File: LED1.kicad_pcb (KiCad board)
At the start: 2 copper layers, 45.7 x 30.5 mm, 11 parts, among them J1 Conn_01x02_Pin, SW1 Tactile_Switch_2-pin - Red, SW2 Tactile_Switch_2-pin - Yellow, SW3 Tactile_Switch_2-pin - Green

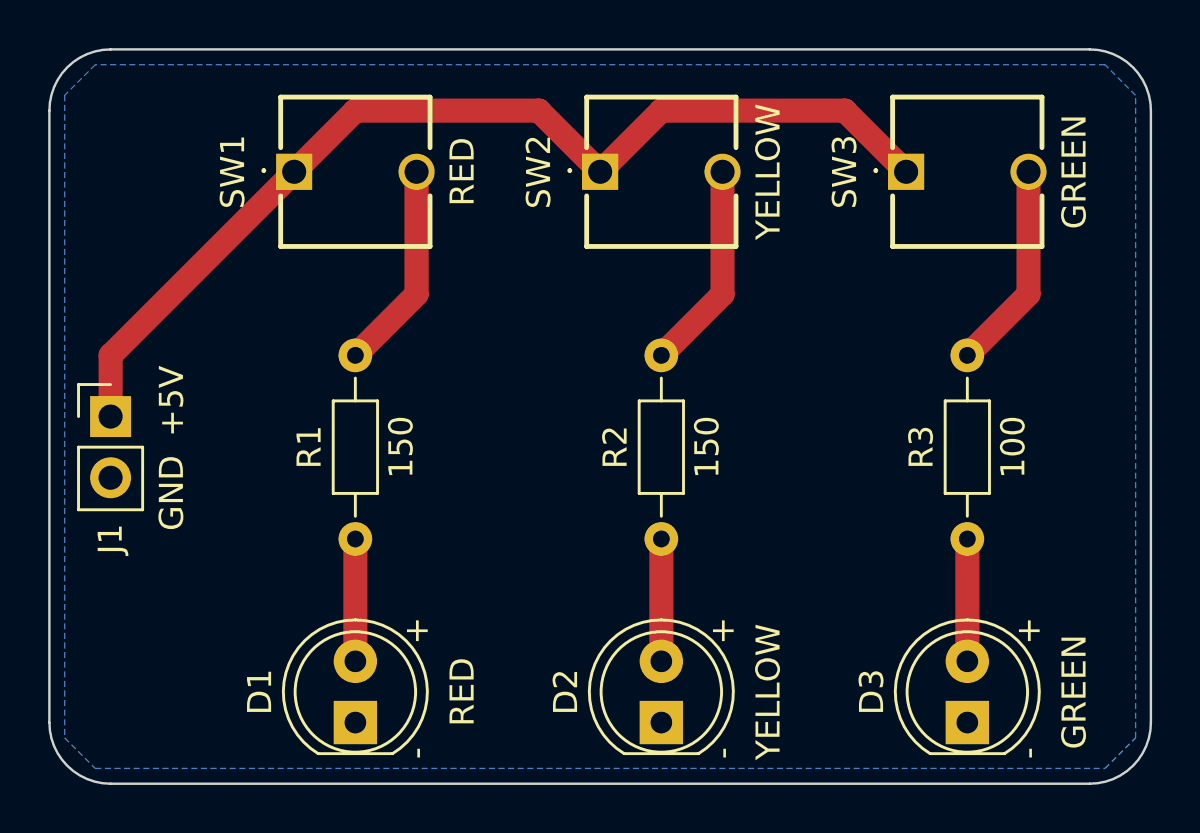
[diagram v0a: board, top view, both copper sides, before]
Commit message: Improved the layout by rotating the tactile switches.
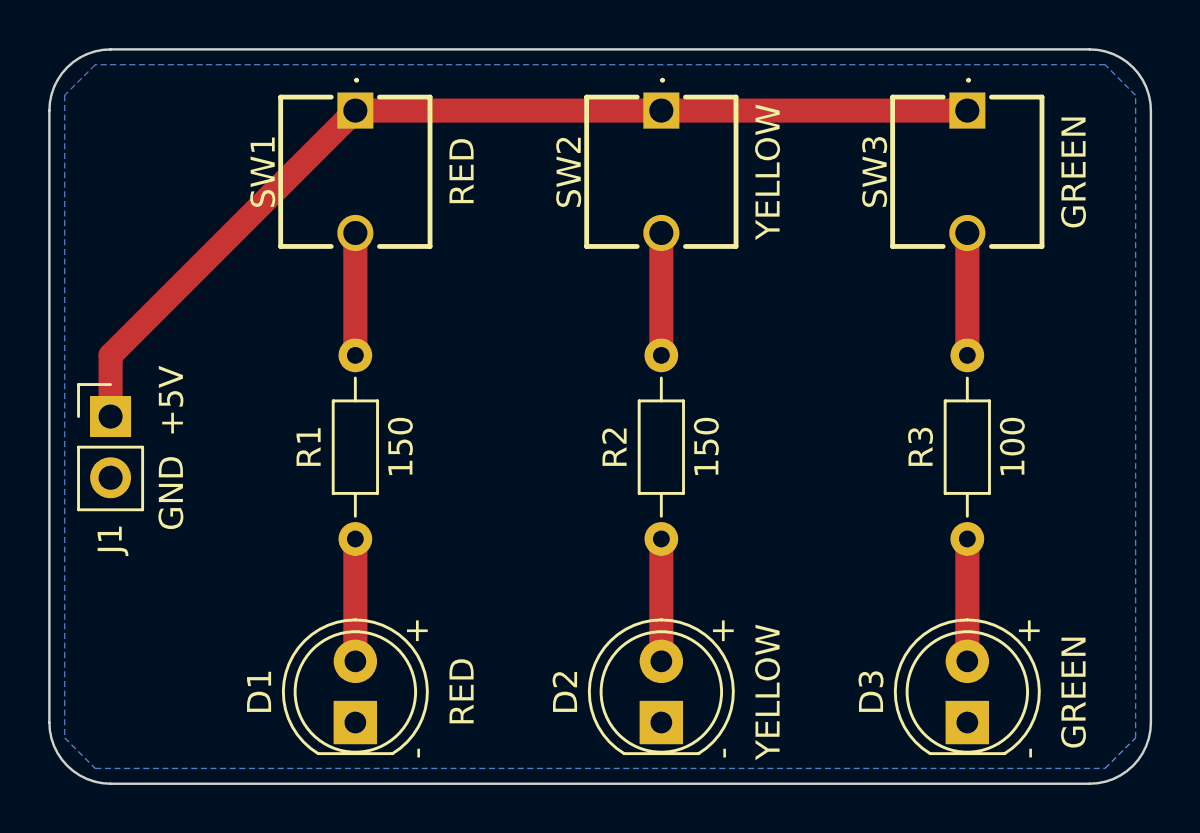
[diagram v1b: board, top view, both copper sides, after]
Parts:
- moved SW1 3.59 mm to (177.8, 58.4), turned to -90 degrees
- moved SW2 3.59 mm to (190.5, 58.4), turned to -90 degrees
- moved SW3 3.59 mm to (203.2, 58.4), turned to -90 degrees
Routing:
- net Net-(R3-Pad1): track 8.67 -> 5.08 mm
- net Net-(R2-Pad1): track 8.67 -> 5.08 mm
- net Net-(R1-Pad1): track 8.67 -> 5.08 mm
- net +5V: track 42.9 -> 42.3 mm
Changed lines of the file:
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@@
   )
   (footprint "Footprints_CJ:Tactile Switch - 6 x 6 mm - 2-pin - Yellow" (layer "F.Cu")
-    (at 187.96 60.96)
+    (at 190.5 58.42 -90)
     (descr "2-pin Tactile Switch 6x6x5 mm - YELLOW")
     (tags "Switch")
@@
     (property "ki_keywords" "Tactile Switch 2-pin Yellow")
     (attr through_hole)
-    (fp_text reference "SW2" (at -2.54 0 90) (layer "F.SilkS")
+    (fp_text reference "SW2" (at 2.54 3.81 90) (layer "F.SilkS")
         (effects (font (size 1 1) (thickness 0.15)))
     )
-    (fp_text value "Tactile_Switch_2-pin - Yellow" (at 2.5 0) (layer "F.SilkS") hide
+    (fp_text value "Tactile_Switch_2-pin - Yellow" (at 2.5 0 90) (layer "F.SilkS") hide
         (effects (font (size 1.27 1.27) (thickness 0.254)))
     )
-    (fp_text user "${REFERENCE}" (at 2.54 0) (layer "F.Fab") hide
+    (fp_text user "${REFERENCE}" (at 2.54 0 90) (layer "F.Fab") hide
         (effects (font (size 1.27 1.27) (thickness 0.254)))
     )
@@
     (fp_line (start 5.64 3.1) (end -0.56 3.1)
       (stroke (width 0.1) (type solid)) (layer "F.Fab"))
-    (pad "1" thru_hole rect (at 0 0) (size 1.5 1.5) (drill 1) (layers "*.Cu" "*.Mask")
+    (pad "1" thru_hole rect (at 0 0 270) (size 1.5 1.5) (drill 1) (layers "*.Cu" "*.Mask")
       (net 4 "+5V") (pintype "passive"))
-    (pad "2" thru_hole circle (at 5.08 0) (size 1.5 1.5) (drill 1) (layers "*.Cu" "*.Mask")
+    (pad "2" thru_hole circle (at 5.08 0 270) (size 1.5 1.5) (drill 1) (layers "*.Cu" "*.Mask")
       (net 7 "Net-(R2-Pad1)") (pintype "passive"))
     (model "E:/OneDrive/Projects/Electronics/KiCad/Libraries/CJ/3D Models/Tactile Switches TH (6mm×6mm -2pin) Yellow.stp"
@@
   )
   (footprint "Footprints_CJ:Tactile Switch - 6 x 6 mm - 2-pin - Red" (layer "F.Cu")
-    (at 175.26 60.96)
+    (at 177.8 58.42 -90)
     (descr "2-pin Tactile Switch 6x6x5 mm - RED")
     (tags "Switch")
@@
     (property "ki_keywords" "Tactile Switch 2-pin Red")
     (attr through_hole)
-    (fp_text reference "SW1" (at -2.54 0 90) (layer "F.SilkS")
+    (fp_text reference "SW1" (at 2.54 3.81 -90) (layer "F.SilkS")
         (effects (font (size 1 1) (thickness 0.15)))
     )
-    (fp_text value "Tactile_Switch_2-pin - Red" (at 2.5 0) (layer "F.SilkS") hide
+    (fp_text value "Tactile_Switch_2-pin - Red" (at 2.5 0 90) (layer "F.SilkS") hide
         (effects (font (size 1.27 1.27) (thickness 0.254)))
     )
-    (fp_text user "${REFERENCE}" (at 2.54 0) (layer "F.Fab") hide
+    (fp_text user "${REFERENCE}" (at 2.54 0 90) (layer "F.Fab") hide
         (effects (font (size 1.27 1.27) (thickness 0.254)))
     )
@@
     (fp_line (start 5.64 3.1) (end -0.56 3.1)
       (stroke (width 0.1) (type solid)) (layer "F.Fab"))
-    (pad "1" thru_hole rect (at 0 0) (size 1.5 1.5) (drill 1) (layers "*.Cu" "*.Mask")
+    (pad "1" thru_hole rect (at 0 0 270) (size 1.5 1.5) (drill 1) (layers "*.Cu" "*.Mask")
       (net 4 "+5V") (pintype "passive"))
-    (pad "2" thru_hole circle (at 5.08 0) (size 1.5 1.5) (drill 1) (layers "*.Cu" "*.Mask")
+    (pad "2" thru_hole circle (at 5.08 0 270) (size 1.5 1.5) (drill 1) (layers "*.Cu" "*.Mask")
       (net 3 "Net-(R1-Pad1)") (pintype "passive"))
     (model "E:/OneDrive/Projects/Electronics/KiCad/Libraries/CJ/3D Models/Tactile Switches TH (6mm×6mm -2pin) Red.stp"
@@
   )
   (footprint "Footprints_CJ:Tactile Switch - 6 x 6 mm - 2-pin - Green" (layer "F.Cu")
-    (at 200.66 60.96)
+    (at 203.2 58.42 -90)
     (descr "2-pin Tactile Switch 6x6x5 mm - GREEN")
     (tags "Switch")
@@
     (property "ki_keywords" "Tactile Switch 2-pin Green")
     (attr through_hole)
-    (fp_text reference "SW3" (at -2.54 0 90) (layer "F.SilkS")
+    (fp_text reference "SW3" (at 2.54 3.81 90) (layer "F.SilkS")
         (effects (font (size 1 1) (thickness 0.15)))
     )
-    (fp_text value "Tactile_Switch_2-pin - Green" (at 2.5 0) (layer "F.SilkS") hide
+    (fp_text value "Tactile_Switch_2-pin - Green" (at 2.5 0 90) (layer "F.SilkS") hide
         (effects (font (size 1.27 1.27) (thickness 0.254)))
     )
-    (fp_text user "${REFERENCE}" (at 2.54 0) (layer "F.Fab") hide
+    (fp_text user "${REFERENCE}" (at 2.54 0 90) (layer "F.Fab") hide
         (effects (font (size 1.27 1.27) (thickness 0.254)))
     )
@@
     (fp_line (start 5.64 3.1) (end -0.56 3.1)
       (stroke (width 0.1) (type solid)) (layer "F.Fab"))
-    (pad "1" thru_hole rect (at 0 0) (size 1.5 1.5) (drill 1) (layers "*.Cu" "*.Mask")
+    (pad "1" thru_hole rect (at 0 0 270) (size 1.5 1.5) (drill 1) (layers "*.Cu" "*.Mask")
       (net 4 "+5V") (pintype "passive"))
-    (pad "2" thru_hole circle (at 5.08 0) (size 1.5 1.5) (drill 1) (layers "*.Cu" "*.Mask")
+    (pad "2" thru_hole circle (at 5.08 0 270) (size 1.5 1.5) (drill 1) (layers "*.Cu" "*.Mask")
       (net 8 "Net-(R3-Pad1)") (pintype "passive"))
     (model "E:/OneDrive/Projects/Electronics/KiCad/Libraries/CJ/3D Models/Tactile Switches TH (6mm×6mm -2pin) Green.stp"
@@
   )
   (segment (start 177.8 76.2) (end 177.8 81.28) (width 1) (layer "F.Cu") (net 2))
-  (segment (start 180.34 66.04) (end 177.8 68.58) (width 1) (layer "F.Cu") (net 3))
-  (segment (start 180.34 60.96) (end 180.34 66.04) (width 1) (layer "F.Cu") (net 3))
-  (segment (start 185.42 58.42) (end 187.96 60.96) (width 1) (layer "F.Cu") (net 4))
+  (segment (start 177.8 63.5) (end 177.8 68.58) (width 1) (layer "F.Cu") (net 3))
+  (segment (start 190.5 58.42) (end 203.2 58.42) (width 1) (layer "F.Cu") (net 4))
+  (segment (start 167.64 68.58) (end 177.8 58.42) (width 1) (layer "F.Cu") (net 4))
+  (segment (start 177.8 58.42) (end 190.5 58.42) (width 1) (layer "F.Cu") (net 4))
   (segment (start 167.64 71.12) (end 167.64 68.58) (width 1) (layer "F.Cu") (net 4))
-  (segment (start 167.64 68.58) (end 175.26 60.96) (width 1) (layer "F.Cu") (net 4))
-  (segment (start 177.8 58.42) (end 185.42 58.42) (width 1) (layer "F.Cu") (net 4))
-  (segment (start 187.96 60.96) (end 190.5 58.42) (width 1) (layer "F.Cu") (net 4))
-  (segment (start 190.5 58.42) (end 198.12 58.42) (width 1) (layer "F.Cu") (net 4))
-  (segment (start 198.12 58.42) (end 200.66 60.96) (width 1) (layer "F.Cu") (net 4))
-  (segment (start 175.26 60.96) (end 177.8 58.42) (width 1) (layer "F.Cu") (net 4))
   (segment (start 190.5 76.2) (end 190.5 81.28) (width 1) (layer "F.Cu") (net 5))
   (segment (start 203.2 76.2) (end 203.2 81.28) (width 1) (layer "F.Cu") (net 6))
-  (segment (start 193.04 60.96) (end 193.04 66.04) (width 1) (layer "F.Cu") (net 7))
-  (segment (start 193.04 66.04) (end 190.5 68.58) (width 1) (layer "F.Cu") (net 7))
-  (segment (start 205.74 60.96) (end 205.74 66.04) (width 1) (layer "F.Cu") (net 8))
-  (segment (start 205.74 66.04) (end 203.2 68.58) (width 1) (layer "F.Cu") (net 8))
+  (segment (start 190.5 63.5) (end 190.5 68.58) (width 1) (layer "F.Cu") (net 7))
+  (segment (start 203.2 63.5) (end 203.2 68.58) (width 1) (layer "F.Cu") (net 8))
   (zone (net 1) (net_name "GND") (layer "B.Cu") (hatch edge 0.5)
     (connect_pads (clearance 0.5))
